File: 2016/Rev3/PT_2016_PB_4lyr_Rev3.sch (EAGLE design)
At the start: 177 parts, among them Q12 2N7002

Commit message: Changed board to 3.3v, added 12v buck protection
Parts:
- removed R12, R16, R18, R20, R22, R24, R26, R28, R29: 249k, SparkFun-Resistors:RESISTOR1206
- removed R14, R17, R19, R21, R23, R25, R27, R30, R31, R9: 499k, SparkFun-Resistors:RESISTOR1206
- removed REY-5V: MURATA_5V_DC-DC_CONVERTER, MRDT-2015-PowerBoard:MURATA_5V_DC-DC_CONVERTER
- added BB-8-5V1: Q_OKI-78SR, MRDT-2015-PowerBoard:Q_OKI-78SR
- added C10, C9: 1uF, resistor:C-USC1206
- added C5: 1nF, resistor:C-USC1206
- added C7: 10uF, resistor:C-USC1206
- added C8: .1uF, resistor:C-USC1206
- added Q1, Q3: Q_IRF7437SMD, MRDT-2015-PowerBoard:Q_IRF7437SMD
- added Q2: 2N7002, SparkFun-DiscreteSemi:MOSFET-NCHANNEL2N7002PW
- added U$13, U$9: LM74670-Q1, LM74670-Q1:LM74670-Q1
- added U$7: UVQ-5/20-D24PB-C, MRDT-2015-PowerBoard:UVQ-5/20-D24PB-C
- R3: value 60kΩ -> 100k 1%
- R4: value 10kΩ -> 10kΩ 1%
- R5: value 249k -> 1k; device SparkFun-Resistors:RESISTOR1206 -> resistor:R-US_R1206
- renumbered 1M to R4, 9.31M to R3
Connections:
- removed net +5V: 5V-INT.R, ACS714-M1.VCC, ACS714-M2.VCC, ACS714-M3.VCC, ACS714-M4.VCC, ACS714-M5.VCC, ACS714-M6.VCC, ACS714-M7.VCC, ACS714-M8.VCC, ACS714CAP-M1.2, ACS714CAP-M2.2, ACS714CAP-M3.2, ACS714CAP-M4.2, ACS714CAP-M5.2, ACS714CAP-M6.2, ACS714CAP-M7.2, ACS714CAP-M8.2, BB-8-5V.VO, C11.2, C47.1, C48.1, C49.1, C6.2, LED5.A, U$1.+5V, U$12.VCC, U$21.VCC, U$24.VCC, U$3.VCC
- removed net IMEAS-12VR: R29.1, U$21.VIOUT
- removed net IMEAS-5VR: R28.1, U$3.VIOUT
- removed net IMEAS-M1R: ACS714-M1.VIOUT, R18.1
- removed net IMEAS-M2R: ACS714-M2.VIOUT, R16.1
- removed net IMEAS-M3R: ACS714-M3.VIOUT, R12.1
- removed net IMEAS-M4R: ACS714-M4.VIOUT, R5.1
- removed net IMEAS-M5R: ACS714-M5.VIOUT, R20.1
- removed net IMEAS-M6R: ACS714-M6.VIOUT, R26.1
- removed net IMEAS-M7R: ACS714-M7.VIOUT, R24.1
- removed net IMEAS-M8R: ACS714-M8.VIOUT, R22.1
- new net 3.3V: 5V-INT.R, ACS714-M1.VCC, ACS714-M2.VCC, ACS714-M3.VCC, ACS714-M4.VCC, ACS714-M5.VCC, ACS714-M6.VCC, ACS714-M7.VCC, ACS714-M8.VCC, ACS714CAP-M1.2, ACS714CAP-M2.2, ACS714CAP-M3.2, ACS714CAP-M4.2, ACS714CAP-M5.2, ACS714CAP-M6.2, ACS714CAP-M7.2, ACS714CAP-M8.2, BB-8-5V.VO, C11.2, C47.1, C48.1, C49.1, C6.2, LED5.A, U$12.VCC, U$21.VCC, U$24.VCC, U$3.VCC
- new net 5V: BB-8-5V1.VO, C5.1, C7.1, C8.1, U$1.+5V
- new net N$1: FINN-12V.+VOUT, Q3.S, U$9.ANODE
- new net N$10: C10.2, U$13.V_CAP_L
- new net N$2: POE-12V.+VOUT, Q1.S, U$13.ANODE
- new net N$3: Q3.G, U$9.GATE_DRIVE, U$9.GATE_PULL_DOWN
- new net N$48: Q2.G, R11.1
- new net N$5: Q1.G, U$13.GATE_DRIVE, U$13.GATE_PULL_DOWN
- new net N$7: C9.1, U$9.V_CAP_H
- new net N$8: C9.2, U$9.V_CAP_L
- new net N$9: C10.1, U$13.V_CAP_H
- net GND: now also BB-8-5V1.GND, C5.2, C7.2, C8.2, Q2.S, R5.2, U$7.-SENSE, U$7.-VIN, U$7.-VOUT; no longer R14.1, R17.1, R19.1, R21.1, R23.1, R25.1, R27.1, R30.1, R31.1, R9.1, REY-5V.-SENSE, REY-5V.-VIN, REY-5V.-VOUT
- net IMEAS-12V: now also U$21.VIOUT; no longer R29.2, R30.2
- net IMEAS-5V: now also U$1.PE2, U$3.VIOUT; no longer R28.2, R31.2, U$1.PE3
- net IMEAS-M1: now also ACS714-M1.VIOUT; no longer R18.2, R19.2
- net IMEAS-M2: now also ACS714-M2.VIOUT; no longer R16.2, R17.2
- net IMEAS-M3: now also ACS714-M3.VIOUT; no longer R12.2, R14.2
- net IMEAS-M4: now also ACS714-M4.VIOUT; no longer R5.2, R9.2
- net IMEAS-M5: now also ACS714-M5.VIOUT; no longer R20.2, R21.2
- net IMEAS-M6: now also ACS714-M6.VIOUT; no longer R26.2, R27.2
- net IMEAS-M7: now also ACS714-M7.VIOUT; no longer R24.2, R25.2
- net IMEAS-M8: now also ACS714-M8.VIOUT; no longer R22.2, R23.2
- net N$114: now also R5.1
- net N$33: now also Q1.D, Q3.D, U$13.CATHODE, U$9.CATHODE; no longer FINN-12V.+VOUT, POE-12V.+VOUT
- net N$43: now also Q2.D, U$7.ON/OFF; no longer R11.1, REY-5V.ON/OFF
- net N$71: now also U$7.+SENSE, U$7.+VOUT; no longer REY-5V.+SENSE, REY-5V.+VOUT
- net VMEAS-VBATT: now also U$1.PE3; no longer U$1.PE2
- net V_BATT: now also BB-8-5V1.VI, U$7.+VIN; no longer REY-5V.+VIN
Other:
- moved on the sheet: ACS714-M1, ACS714-M2, ACS714-M3, ACS714-M4, ACS714-M5, ACS714-M6, ACS714-M7, ACS714-M8, ACS714CAP-M1, ACS714CAP-M2, ACS714CAP-M3, ACS714CAP-M4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

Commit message: Moved around 12v bucks, routed ORing mosfet circuits
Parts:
- removed R1, R6: 120 Ohm, SparkFun-Passives:RESISTOR1206
- removed U$12: MAX3077, MAX3077:MAX3077
- removed U$6: RJ45FCI-54602-908LF, MRDT-2015-General:RJ45FCI-54602-908LF
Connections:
- removed net REC+: R1.1, U$12.A, U$6.1
- removed net REC-: R1.2, U$12.B, U$6.2
- removed net TRANS+: R6.2, U$12.Y, U$6.3
- removed net TRANS-: R6.1, U$12.Z, U$6.6
- net 3.3V: no longer 5V-INT.R, LED5.A, U$12.VCC
- net 5V: now also 5V-INT.R, LED5.A
- net GND: no longer U$12.GND, U$6.7, U$6.8
- net N$1: now also C20.1
- net N$2: now also C19.1
- net N$33: no longer C19.1, C20.1
- net RX2: no longer U$12.R0
- net TX2: no longer U$12.DI
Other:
- moved on the sheet: C19, C20

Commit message: Updated part sizes
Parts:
- BOTAPP-M1, BOTAPP-M2, BOTAPP-M3, BOTAPP-M4, BOTAPP-M5, BOTAPP-M6, BOTAPP-M7, BOTAPP-M8, U$28, U$29: value ANDERSON_POWERPOLEPP45_PCB_HORIZ_RIGHT -> APPPP45_PCB_HORIZ_RIGHT; device MRDT-Connectors:ANDERSON_POWERPOLEPP45_PCB_HORIZ_RIGHT -> MRDT-Connectors:APPPP45_PCB_HORIZ_RIGHT
- TOPAPP-M1, TOPAPP-M2, TOPAPP-M3, TOPAPP-M4, TOPAPP-M5, TOPAPP-M6, TOPAPP-M7, TOPAPP-M8, U$26, U$27: value ANDERSON_POWERPOLEPP45_PCB_HORIZ_RIGHT_2HIGH -> APPPP45_PCB_HORIZ_RIGHT_2HIGH; device MRDT-Connectors:ANDERSON_POWERPOLEPP45_PCB_HORIZ_RIGHT_2HIGH -> MRDT-Connectors:APPPP45_PCB_HORIZ_RIGHT_2HIGH
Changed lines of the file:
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@@
 <part name="R7" library="SparkFun-Passives" deviceset="RESISTOR" device="1206" value="120 Ohm"/>
 <part name="GND15" library="SparkFun-Aesthetics" deviceset="GND" device=""/>
-<part name="BOTAPP-M1" library="MRDT-Connectors" deviceset="ANDERSON_POWERPOLE" device="PP45_PCB_HORIZ_RIGHT"/>
-<part name="TOPAPP-M1" library="MRDT-Connectors" deviceset="ANDERSON_POWERPOLE" device="PP45_PCB_HORIZ_RIGHT_2HIGH" value="ANDERSON_POWERPOLEPP45_PCB_HORIZ_RIGHT_2HIGH"/>
+<part name="BOTAPP-M1" library="MRDT-Connectors" deviceset="APP" device="PP45_PCB_HORIZ_RIGHT"/>
+<part name="TOPAPP-M1" library="MRDT-Connectors" deviceset="APP" device="PP45_PCB_HORIZ_RIGHT_2HIGH" value="APPPP45_PCB_HORIZ_RIGHT_2HIGH"/>
 <part name="U$41" library="MRDT-Connectors" deviceset="APP_MOUTING_WING" device="HORIZ"/>
 <part name="U$42" library="MRDT-Connectors" deviceset="APP_MOUTING_WING" device="HORIZ"/>
 <part name="U$25" library="MRDT-Connectors" deviceset="APP_MOUTING_WING" device="HORIZ"/>
-<part name="U$26" library="MRDT-Connectors" deviceset="ANDERSON_POWERPOLE" device="PP45_PCB_HORIZ_RIGHT_2HIGH" value="ANDERSON_POWERPOLEPP45_PCB_HORIZ_RIGHT_2HIGH"/>
-<part name="U$27" library="MRDT-Connectors" deviceset="ANDERSON_POWERPOLE" device="PP45_PCB_HORIZ_RIGHT_2HIGH" value="ANDERSON_POWERPOLEPP45_PCB_HORIZ_RIGHT_2HIGH"/>
-<part name="U$28" library="MRDT-Connectors" deviceset="ANDERSON_POWERPOLE" device="PP45_PCB_HORIZ_RIGHT" value="ANDERSON_POWERPOLEPP45_PCB_HORIZ_RIGHT"/>
-<part name="U$29" library="MRDT-Connectors" deviceset="ANDERSON_POWERPOLE" device="PP45_PCB_HORIZ_RIGHT" value="ANDERSON_POWERPOLEPP45_PCB_HORIZ_RIGHT"/>
+<part name="U$26" library="MRDT-Connectors" deviceset="APP" device="PP45_PCB_HORIZ_RIGHT_2HIGH" value="APPPP45_PCB_HORIZ_RIGHT_2HIGH"/>
+<part name="U$27" library="MRDT-Connectors" deviceset="APP" device="PP45_PCB_HORIZ_RIGHT_2HIGH" value="APPPP45_PCB_HORIZ_RIGHT_2HIGH"/>
+<part name="U$28" library="MRDT-Connectors" deviceset="APP" device="PP45_PCB_HORIZ_RIGHT" value="APPPP45_PCB_HORIZ_RIGHT"/>
+<part name="U$29" library="MRDT-Connectors" deviceset="APP" device="PP45_PCB_HORIZ_RIGHT" value="APPPP45_PCB_HORIZ_RIGHT"/>
 <part name="C13" library="resistor" deviceset="C-US" device="C1206" value="1uF"/>
 <part name="GND36" library="SparkFun-Aesthetics" deviceset="GND" device=""/>
@@
 <part name="FILTERCAP-M2" library="resistor" deviceset="C-US" device="C1206" value="1nF"/>
 <part name="GND33" library="SparkFun-Aesthetics" deviceset="GND" device=""/>
-<part name="BOTAPP-M2" library="MRDT-Connectors" deviceset="ANDERSON_POWERPOLE" device="PP45_PCB_HORIZ_RIGHT"/>
-<part name="TOPAPP-M2" library="MRDT-Connectors" deviceset="ANDERSON_POWERPOLE" device="PP45_PCB_HORIZ_RIGHT_2HIGH" value="ANDERSON_POWERPOLEPP45_PCB_HORIZ_RIGHT_2HIGH"/>
+<part name="BOTAPP-M2" library="MRDT-Connectors" deviceset="APP" device="PP45_PCB_HORIZ_RIGHT"/>
+<part name="TOPAPP-M2" library="MRDT-Connectors" deviceset="APP" device="PP45_PCB_HORIZ_RIGHT_2HIGH" value="APPPP45_PCB_HORIZ_RIGHT_2HIGH"/>
 <part name="SUPPLY9" library="SparkFun-Aesthetics" deviceset="V_BATT" device=""/>
 <part name="FET-M3" library="MRDT-2015-PowerBoard" deviceset="Q_IRF*7437" device="SMD" value="Q_IRFS7437PbF"/>
@@
 <part name="FILTERCAP-M3" library="resistor" deviceset="C-US" device="C1206" value="1nF"/>
 <part name="GND51" library="SparkFun-Aesthetics" deviceset="GND" device=""/>
-<part name="BOTAPP-M3" library="MRDT-Connectors" deviceset="ANDERSON_POWERPOLE" device="PP45_PCB_HORIZ_RIGHT"/>
-<part name="TOPAPP-M3" library="MRDT-Connectors" deviceset="ANDERSON_POWERPOLE" device="PP45_PCB_HORIZ_RIGHT_2HIGH" value="ANDERSON_POWERPOLEPP45_PCB_HORIZ_RIGHT_2HIGH"/>
+<part name="BOTAPP-M3" library="MRDT-Connectors" deviceset="APP" device="PP45_PCB_HORIZ_RIGHT"/>
+<part name="TOPAPP-M3" library="MRDT-Connectors" deviceset="APP" device="PP45_PCB_HORIZ_RIGHT_2HIGH" value="APPPP45_PCB_HORIZ_RIGHT_2HIGH"/>
 <part name="SUPPLY10" library="SparkFun-Aesthetics" deviceset="V_BATT" device=""/>
 <part name="FET-M4" library="MRDT-2015-PowerBoard" deviceset="Q_IRF*7437" device="SMD" value="Q_IRFS7437PbF"/>
@@
 <part name="FILTERCAP-M4" library="resistor" deviceset="C-US" device="C1206" value="1nF"/>
 <part name="GND57" library="SparkFun-Aesthetics" deviceset="GND" device=""/>
-<part name="BOTAPP-M4" library="MRDT-Connectors" deviceset="ANDERSON_POWERPOLE" device="PP45_PCB_HORIZ_RIGHT"/>
-<part name="TOPAPP-M4" library="MRDT-Connectors" deviceset="ANDERSON_POWERPOLE" device="PP45_PCB_HORIZ_RIGHT_2HIGH" value="ANDERSON_POWERPOLEPP45_PCB_HORIZ_RIGHT_2HIGH"/>
+<part name="BOTAPP-M4" library="MRDT-Connectors" deviceset="APP" device="PP45_PCB_HORIZ_RIGHT"/>
+<part name="TOPAPP-M4" library="MRDT-Connectors" deviceset="APP" device="PP45_PCB_HORIZ_RIGHT_2HIGH" value="APPPP45_PCB_HORIZ_RIGHT_2HIGH"/>
 <part name="SUPPLY11" library="SparkFun-Aesthetics" deviceset="V_BATT" device=""/>
 <part name="FET-M5" library="MRDT-2015-PowerBoard" deviceset="Q_IRF*7437" device="SMD" value="Q_IRFS7437PbF"/>
@@
 <part name="FILTERCAP-M5" library="resistor" deviceset="C-US" device="C1206" value="1nF"/>
 <part name="GND63" library="SparkFun-Aesthetics" deviceset="GND" device=""/>
-<part name="BOTAPP-M5" library="MRDT-Connectors" deviceset="ANDERSON_POWERPOLE" device="PP45_PCB_HORIZ_RIGHT"/>
-<part name="TOPAPP-M5" library="MRDT-Connectors" deviceset="ANDERSON_POWERPOLE" device="PP45_PCB_HORIZ_RIGHT_2HIGH" value="ANDERSON_POWERPOLEPP45_PCB_HORIZ_RIGHT_2HIGH"/>
+<part name="BOTAPP-M5" library="MRDT-Connectors" deviceset="APP" device="PP45_PCB_HORIZ_RIGHT"/>
+<part name="TOPAPP-M5" library="MRDT-Connectors" deviceset="APP" device="PP45_PCB_HORIZ_RIGHT_2HIGH" value="APPPP45_PCB_HORIZ_RIGHT_2HIGH"/>
 <part name="SUPPLY12" library="SparkFun-Aesthetics" deviceset="V_BATT" device=""/>
 <part name="FET-M6" library="MRDT-2015-PowerBoard" deviceset="Q_IRF*7437" device="SMD" value="Q_IRFS7437PbF"/>
@@
 <part name="FILTERCAP-M6" library="resistor" deviceset="C-US" device="C1206" value="1nF"/>
 <part name="GND69" library="SparkFun-Aesthetics" deviceset="GND" device=""/>
-<part name="BOTAPP-M6" library="MRDT-Connectors" deviceset="ANDERSON_POWERPOLE" device="PP45_PCB_HORIZ_RIGHT"/>
-<part name="TOPAPP-M6" library="MRDT-Connectors" deviceset="ANDERSON_POWERPOLE" device="PP45_PCB_HORIZ_RIGHT_2HIGH" value="ANDERSON_POWERPOLEPP45_PCB_HORIZ_RIGHT_2HIGH"/>
+<part name="BOTAPP-M6" library="MRDT-Connectors" deviceset="APP" device="PP45_PCB_HORIZ_RIGHT"/>
+<part name="TOPAPP-M6" library="MRDT-Connectors" deviceset="APP" device="PP45_PCB_HORIZ_RIGHT_2HIGH" value="APPPP45_PCB_HORIZ_RIGHT_2HIGH"/>
 <part name="SUPPLY13" library="SparkFun-Aesthetics" deviceset="V_BATT" device=""/>
 <part name="FET-M7" library="MRDT-2015-PowerBoard" deviceset="Q_IRF*7437" device="SMD" value="Q_IRFS7437PbF"/>
@@
 <part name="FILTERCAP-M7" library="resistor" deviceset="C-US" device="C1206" value="1nF"/>
 <part name="GND79" library="SparkFun-Aesthetics" deviceset="GND" device=""/>
-<part name="BOTAPP-M7" library="MRDT-Connectors" deviceset="ANDERSON_POWERPOLE" device="PP45_PCB_HORIZ_RIGHT"/>
-<part name="TOPAPP-M7" library="MRDT-Connectors" deviceset="ANDERSON_POWERPOLE" device="PP45_PCB_HORIZ_RIGHT_2HIGH" value="ANDERSON_POWERPOLEPP45_PCB_HORIZ_RIGHT_2HIGH"/>
+<part name="BOTAPP-M7" library="MRDT-Connectors" deviceset="APP" device="PP45_PCB_HORIZ_RIGHT"/>
+<part name="TOPAPP-M7" library="MRDT-Connectors" deviceset="APP" device="PP45_PCB_HORIZ_RIGHT_2HIGH" value="APPPP45_PCB_HORIZ_RIGHT_2HIGH"/>
 <part name="SUPPLY15" library="SparkFun-Aesthetics" deviceset="V_BATT" device=""/>
 <part name="FET-M8" library="MRDT-2015-PowerBoard" deviceset="Q_IRF*7437" device="SMD" value="Q_IRFS7437PbF"/>
@@
 <part name="FILTERCAP-M8" library="resistor" deviceset="C-US" device="C1206" value="1nF"/>
 <part name="GND85" library="SparkFun-Aesthetics" deviceset="GND" device=""/>
-<part name="BOTAPP-M8" library="MRDT-Connectors" deviceset="ANDERSON_POWERPOLE" device="PP45_PCB_HORIZ_RIGHT"/>
-<part name="TOPAPP-M8" library="MRDT-Connectors" deviceset="ANDERSON_POWERPOLE" device="PP45_PCB_HORIZ_RIGHT_2HIGH" value="ANDERSON_POWERPOLEPP45_PCB_HORIZ_RIGHT_2HIGH"/>
+<part name="BOTAPP-M8" library="MRDT-Connectors" deviceset="APP" device="PP45_PCB_HORIZ_RIGHT"/>
+<part name="TOPAPP-M8" library="MRDT-Connectors" deviceset="APP" device="PP45_PCB_HORIZ_RIGHT_2HIGH" value="APPPP45_PCB_HORIZ_RIGHT_2HIGH"/>
 <part name="U$1" library="MRDT-2015-General" deviceset="TIVA-C-CONNECTED" device=""/>
 <part name="U$2" library="MRDT-Connectors" deviceset="APP_MOUTING_WING" device="HORIZ"/>
@@
 <instance part="U$4" gate="G$1" x="-162.56" y="86.36"/>
 <instance part="U$5" gate="G$1" x="-320.04" y="-55.88"/>
-<instance part="U$8" gate="G$1" x="-162.56" y="68.58"/>
-<instance part="U$10" gate="G$1" x="-149.86" y="68.58"/>
-<instance part="U$11" gate="G$1" x="-162.56" y="60.96"/>
+<instance part="U$8" gate="G$1" x="-149.86" y="86.36"/>
+<instance part="U$10" gate="G$1" x="-149.86" y="78.74"/>
+<instance part="U$11" gate="G$1" x="-162.56" y="78.74"/>
 <instance part="U$7" gate="G$1" x="15.24" y="129.54"/>
 <instance part="SUPPLY18" gate="G$1" x="-22.86" y="-30.48"/>

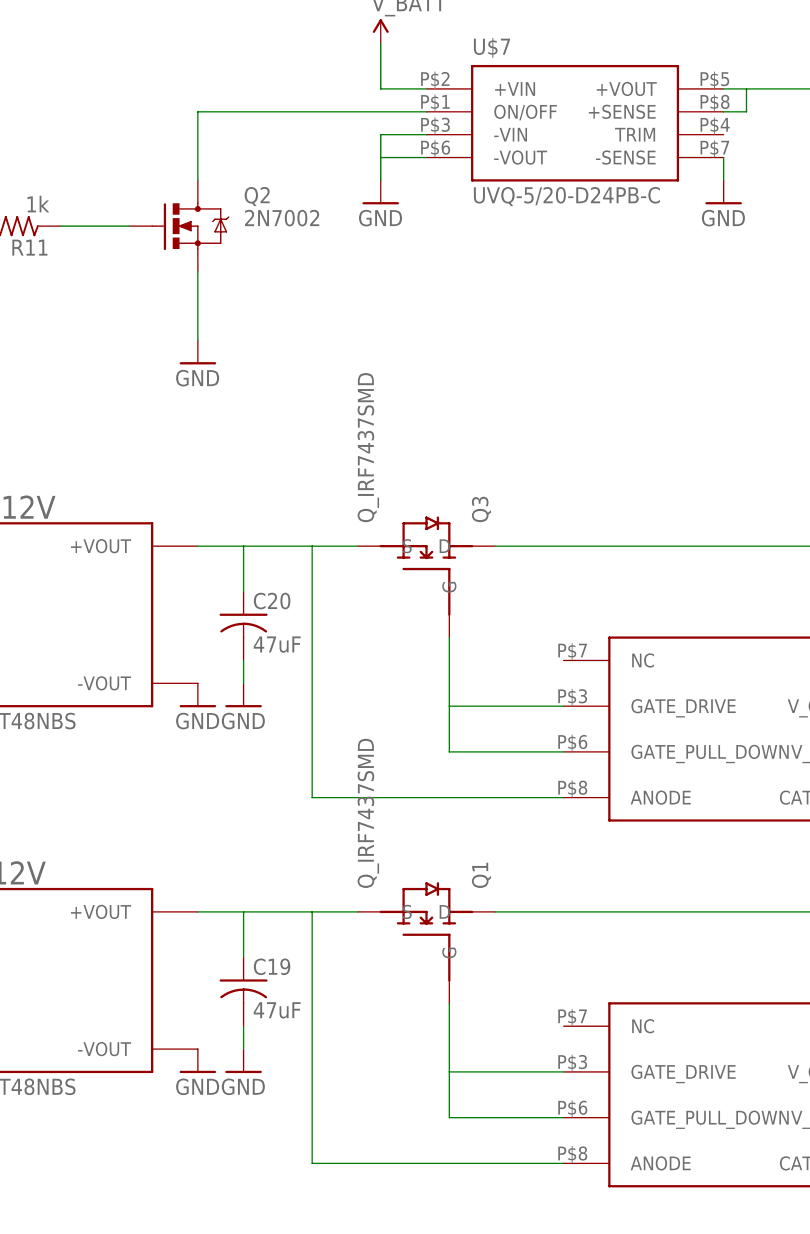
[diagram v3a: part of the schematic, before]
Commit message: Changed ORing FETs to DPAK
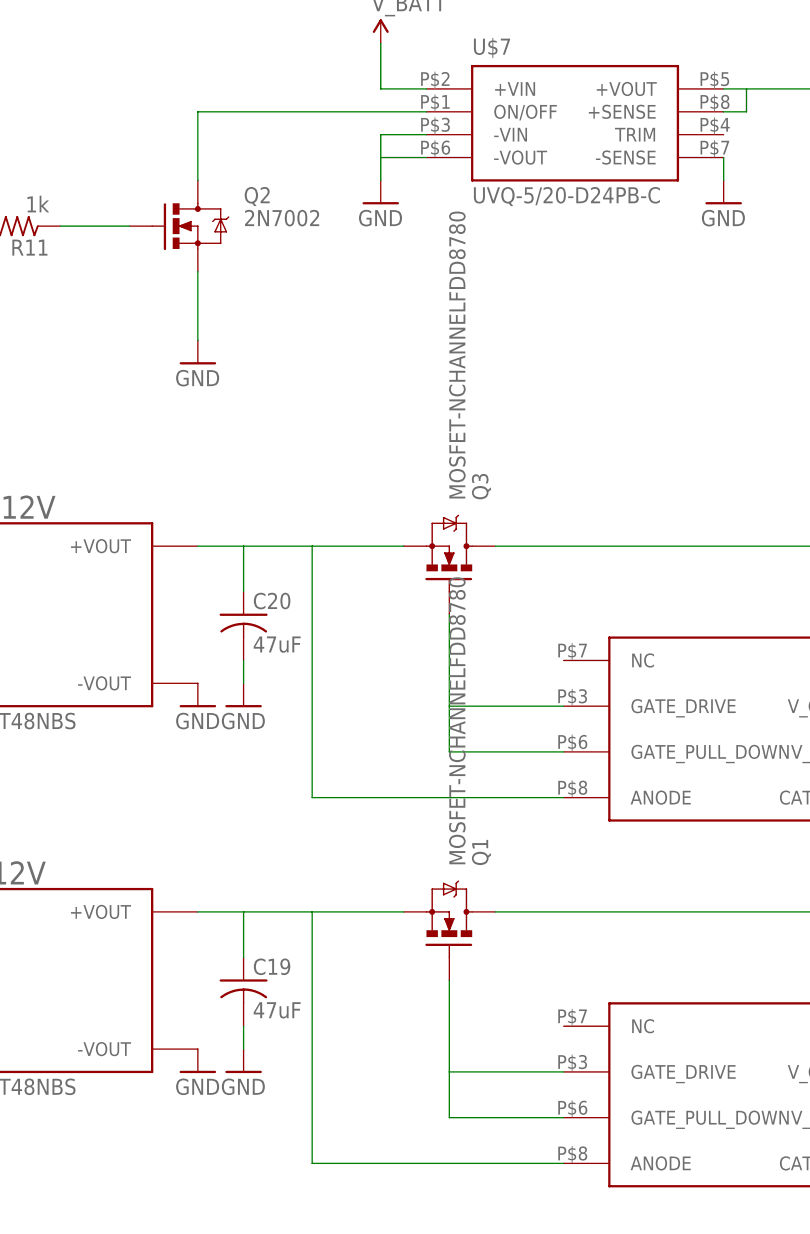
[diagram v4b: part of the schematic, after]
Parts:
- Q1, Q3: value Q_IRF7437SMD -> MOSFET-NCHANNELFDD8780; device MRDT-2015-PowerBoard:Q_IRF7437SMD -> SparkFun-DiscreteSemi:MOSFET-NCHANNELFDD8780
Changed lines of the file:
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@@
 <part name="U$9" library="LM74670-Q1" deviceset="LM74670-Q1" device=""/>
 <part name="U$13" library="LM74670-Q1" deviceset="LM74670-Q1" device=""/>
-<part name="Q1" library="MRDT-2015-PowerBoard" deviceset="Q_IRF*7437" device="SMD"/>
-<part name="Q3" library="MRDT-2015-PowerBoard" deviceset="Q_IRF*7437" device="SMD"/>
+<part name="Q1" library="SparkFun-DiscreteSemi" deviceset="MOSFET-NCHANNEL" device="FDD8780"/>
+<part name="Q3" library="SparkFun-DiscreteSemi" deviceset="MOSFET-NCHANNEL" device="FDD8780"/>
 <part name="C9" library="resistor" deviceset="C-US" device="C1206" value="1uF"/>
 <part name="C10" library="resistor" deviceset="C-US" device="C1206" value="1uF"/>
@@
 <instance part="U$9" gate="G$1" x="35.56" y="58.42"/>
 <instance part="U$13" gate="G$1" x="35.56" y="17.78"/>
-<instance part="Q1" gate="G$1" x="0" y="38.1" rot="MR90"/>
-<instance part="Q3" gate="G$1" x="0" y="78.74" rot="MR90"/>
+<instance part="Q1" gate="G$1" x="2.54" y="40.64" rot="MR90"/>
+<instance part="Q3" gate="G$1" x="2.54" y="81.28" rot="MR90"/>
 <instance part="C9" gate="G$1" x="63.5" y="60.96"/>
 <instance part="C10" gate="G$1" x="63.5" y="20.32"/>
@@
 <pinref part="U$9" gate="G$1" pin="ANODE"/>
 <wire x1="-20.32" y1="81.28" x2="-12.7" y2="81.28" width="0.1524" layer="91"/>
-<wire x1="-12.7" y1="81.28" x2="-7.62" y2="81.28" width="0.1524" layer="91"/>
+<wire x1="-12.7" y1="81.28" x2="-2.54" y2="81.28" width="0.1524" layer="91"/>
 <wire x1="15.24" y1="53.34" x2="-12.7" y2="53.34" width="0.1524" layer="91"/>
 <wire x1="-12.7" y1="53.34" x2="-12.7" y2="81.28" width="0.1524" layer="91"/>
@@
 <pinref part="U$13" gate="G$1" pin="ANODE"/>
 <wire x1="-20.32" y1="40.64" x2="-12.7" y2="40.64" width="0.1524" layer="91"/>
-<wire x1="-12.7" y1="40.64" x2="-7.62" y2="40.64" width="0.1524" layer="91"/>
+<wire x1="-12.7" y1="40.64" x2="-2.54" y2="40.64" width="0.1524" layer="91"/>
 <wire x1="15.24" y1="12.7" x2="-12.7" y2="12.7" width="0.1524" layer="91"/>
 <wire x1="-12.7" y1="12.7" x2="-12.7" y2="40.64" width="0.1524" layer="91"/>
@@
 <wire x1="2.54" y1="58.42" x2="2.54" y2="63.5" width="0.1524" layer="91"/>
 <pinref part="U$9" gate="G$1" pin="GATE_DRIVE"/>
-<wire x1="2.54" y1="63.5" x2="2.54" y2="71.12" width="0.1524" layer="91"/>
+<wire x1="2.54" y1="63.5" x2="2.54" y2="73.66" width="0.1524" layer="91"/>
 <wire x1="15.24" y1="63.5" x2="2.54" y2="63.5" width="0.1524" layer="91"/>
 </segment>
@@
 <wire x1="15.24" y1="17.78" x2="2.54" y2="17.78" width="0.1524" layer="91"/>
 <wire x1="2.54" y1="17.78" x2="2.54" y2="22.86" width="0.1524" layer="91"/>
-<wire x1="2.54" y1="30.48" x2="2.54" y2="22.86" width="0.1524" layer="91"/>
+<wire x1="2.54" y1="33.02" x2="2.54" y2="22.86" width="0.1524" layer="91"/>
 <pinref part="U$13" gate="G$1" pin="GATE_DRIVE"/>
 <wire x1="2.54" y1="22.86" x2="15.24" y2="22.86" width="0.1524" layer="91"/>
